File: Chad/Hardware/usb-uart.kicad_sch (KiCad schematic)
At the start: 27 parts, among them J3 USB_C_Receptacle_USB2.0, U3 INTERFACE-CP2102-GMR(QFN28), U6 RT9025-25GSP, U7 LTC4411

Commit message: Implemented design review feedback
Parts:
- C24: value 0.1uF -> 10uF
- renumbered D5 to USBLED1
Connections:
- net +3V3: now also R19.2
- net GND: no longer R19.2
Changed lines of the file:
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@@
+    (stroke (width 0) (type default) (color 0 0 0 0))
+  )
+  (wire (pts (xy 210.82 120.65) (xy 210.82 125.73))
     (stroke (width 0) (type default) (color 0 0 0 0))
   )
@@
   )
   (wire (pts (xy 208.28 102.87) (xy 215.9 102.87))
+    (stroke (width 0) (type default) (color 0 0 0 0))
+  )
+  (wire (pts (xy 210.82 125.73) (xy 205.74 125.73))
     (stroke (width 0) (type default) (color 0 0 0 0))
   )
@@
   (symbol (lib_id "Device:LED_Small") (at 162.56 92.71 180) (unit 1)
     (in_bom yes) (on_board yes)
-    (property "Reference" "D5" (id 0) (at 162.56 87.503 0))
+    (property "Reference" "USBLED1" (id 0) (at 162.56 87.503 0))
     (property "Value" "USB_LED" (id 1) (at 162.56 89.8144 0))
     (property "Footprint" "LED_SMD:LED_0603_1608Metric" (id 2) (at 162.56 92.71 90)
@@
     (pin "1")
   )
-  (symbol (lib_id "power:GND") (at 210.82 120.65 0) (unit 1)
-    (in_bom yes) (on_board yes) (fields_autoplaced)
-    (property "Reference" "#PWR013" (id 0) (at 210.82 127 0)
-      (effects (font (size 1.27 1.27)) hide)
-    )
-    (property "Value" "GND" (id 1) (at 210.82 125.73 0))
-    (property "Footprint" "" (id 2) (at 210.82 120.65 0)
-      (effects (font (size 1.27 1.27)) hide)
-    )
-    (property "Datasheet" "" (id 3) (at 210.82 120.65 0)
-      (effects (font (size 1.27 1.27)) hide)
-    )
-    (pin "1")
-  )
   (symbol (lib_id "Device:R_Small") (at 219.71 115.57 0) (unit 1)
     (in_bom yes) (on_board yes)
@@
     (pin "2")
   )
+  (symbol (lib_id "power:+3.3V") (at 205.74 125.73 0) (unit 1)
+    (in_bom yes) (on_board yes) (fields_autoplaced)
+    (property "Reference" "#PWR0115" (id 0) (at 205.74 129.54 0)
+      (effects (font (size 1.27 1.27)) hide)
+    )
+    (property "Value" "+3.3V" (id 1) (at 205.74 122.1542 0))
+    (property "Footprint" "" (id 2) (at 205.74 125.73 0)
+      (effects (font (size 1.27 1.27)) hide)
+    )
+    (property "Datasheet" "" (id 3) (at 205.74 125.73 0)
+      (effects (font (size 1.27 1.27)) hide)
+    )
+    (pin "1")
+  )
   (symbol (lib_id "Device:C_Small") (at 215.9 106.68 180) (unit 1)
     (in_bom yes) (on_board yes)
@@
       (effects (font (size 1.27 1.27)) (justify right))
     )
-    (property "Value" "0.1uF" (id 1) (at 209.0797 108.2478 0)
-      (effects (font (size 1.27 1.27)) (justify right))
-    )
+    (property "Value" "10uF" (id 1) (at 209.0797 108.2478 0)
+      (effects (font (size 1.27 1.27)) (justify right))
+    )

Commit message: Changed LDO footprint to include exposed pad
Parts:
- U6: footprint Package_SO:SOP-8_3.9x4.9mm_P1.27mm -> iclr:SOIC127P599X175-9N
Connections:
- net GND: now also U6.9 (GND)
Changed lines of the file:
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@@
   (symbol (lib_id "iclr:RT9025-25GSP") (at 198.12 101.6 0) (unit 1)
     (in_bom yes) (on_board yes) (fields_autoplaced)
-    (property "Reference" "U6" (id 0) (at 198.12 95.25 0))
-    (property "Value" "RT9025-25GSP" (id 1) (at 198.12 97.79 0))
-    (property "Footprint" "Package_SO:SOP-8_3.9x4.9mm_P1.27mm" (id 2) (at 198.12 96.52 0)
+    (property "Reference" "U6" (id 0) (at 198.12 96.7572 0))
+    (property "Value" "RT9025-25GSP" (id 1) (at 198.12 99.2941 0))
+    (property "Footprint" "iclr:SOIC127P599X175-9N" (id 2) (at 198.12 96.52 0)
       (effects (font (size 1.27 1.27)) hide)
     )
@@
     (pin "7")
     (pin "8")
+    (pin "9")
   )
   (symbol (lib_id "power:GND") (at 219.71 118.11 0) (unit 1)

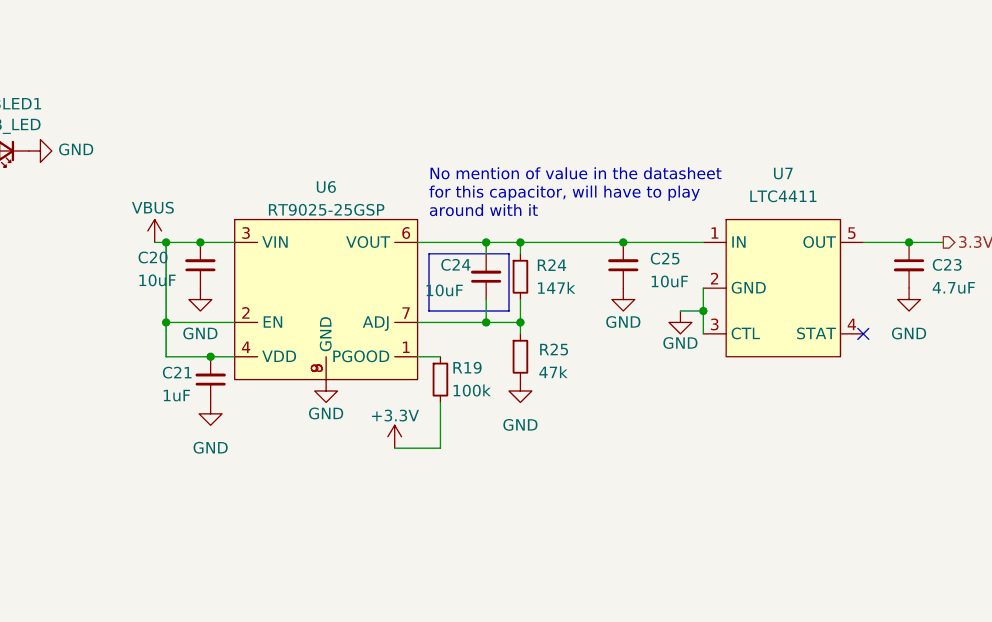
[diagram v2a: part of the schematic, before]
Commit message: change resistor values for new LDO
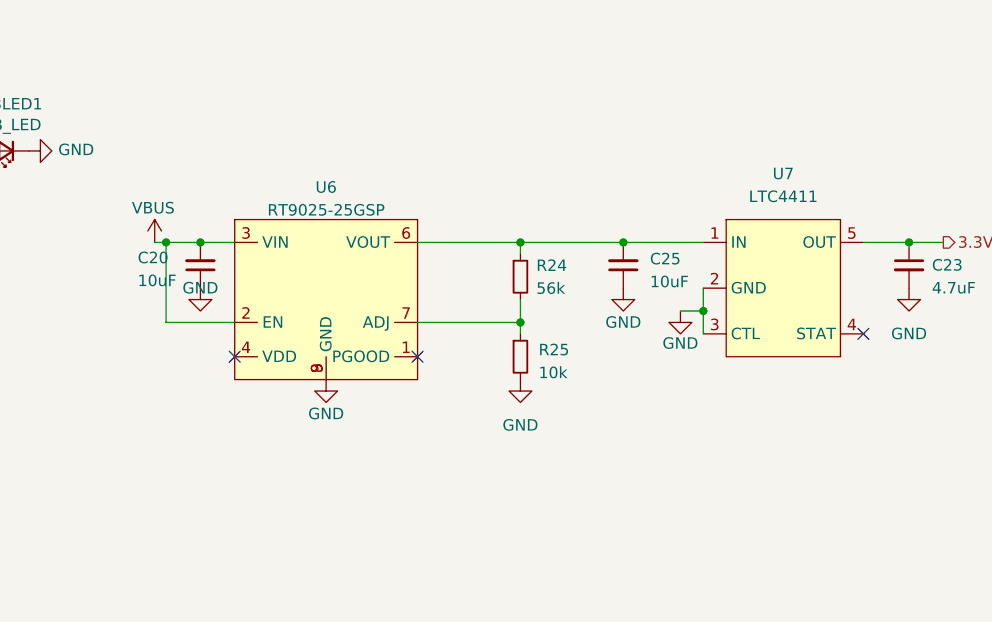
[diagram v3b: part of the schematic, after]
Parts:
- removed C21: 1uF, Capacitor_SMD:C_0603_1608Metric, symbol Device:C_Small
- removed C24: 10uF, Capacitor_SMD:C_0603_1608Metric, symbol Device:C_Small
- removed R19: 100k, Resistor_SMD:R_0603_1608Metric, symbol Device:R_Small
- R24: value 147k -> 56k
- R25: value 47k -> 10k
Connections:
- net VBUS: no longer U6.4 (VDD)
- no-connect marks 21 -> 23
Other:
- note removed: "No mention of value in the datasheet for this capacitor, will have to play around with it"
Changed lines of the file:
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@@
   (junction (at 97.79 52.07) (diameter 0) (color 0 0 0 0)
   )
-  (junction (at 185.2878 115.57) (diameter 0) (color 0 0 0 0)
-  )
   (junction (at 184.15 102.87) (diameter 0) (color 0 0 0 0)
   )
@@
   (junction (at 95.25 52.07) (diameter 0) (color 0 0 0 0)
   )
-  (junction (at 180.34 111.76) (diameter 0) (color 0 0 0 0)
-  )
   (junction (at 102.87 54.61) (diameter 0) (color 0 0 0 0)
   )
   (junction (at 219.71 102.87) (diameter 0) (color 0 0 0 0)
   )
-  (junction (at 215.9 102.87) (diameter 0) (color 0 0 0 0)
-  )
   (junction (at 111.76 44.45) (diameter 0) (color 0 0 0 0)
   )
@@
   )
   (junction (at 113.03 54.61) (diameter 0) (color 0 0 0 0)
-  )
-  (junction (at 215.9 111.76) (diameter 0) (color 0 0 0 0)
   )
   (no_connect (at 161.29 52.07))
@@
   (no_connect (at 161.29 54.61))
   (no_connect (at 115.57 116.84))
+  (no_connect (at 208.28 115.57))
+  (no_connect (at 187.96 115.57))
   (no_connect (at 135.89 26.67))
   (no_connect (at 148.59 67.31))
@@
     (stroke (width 0) (type default) (color 0 0 0 0))
   )
-  (wire (pts (xy 210.82 120.65) (xy 210.82 125.73))
-    (stroke (width 0) (type default) (color 0 0 0 0))
-  )
   (wire (pts (xy 113.03 58.42) (xy 113.03 54.61))
     (stroke (width 0) (type default) (color 0 0 0 0))
@@
     (stroke (width 0) (type default) (color 0 0 0 0))
   )
-  (polyline (pts (xy 209.55 104.14) (xy 218.44 104.14))
-    (stroke (width 0) (type default) (color 0 0 0 0))
-  )
   (wire (pts (xy 107.95 63.5) (xy 107.95 64.77))
     (stroke (width 0) (type default) (color 0 0 0 0))
   )
-  (wire (pts (xy 185.2878 115.57) (xy 187.96 115.57))
-    (stroke (width 0) (type default) (color 0 0 0 0))
-  )
   (wire (pts (xy 96.52 127) (xy 96.52 130.81))
     (stroke (width 0) (type default) (color 0 0 0 0))
@@
     (stroke (width 0) (type default) (color 0 0 0 0))
   )
-  (wire (pts (xy 208.28 111.76) (xy 215.9 111.76))
-    (stroke (width 0) (type default) (color 0 0 0 0))
-  )
   (wire (pts (xy 115.57 102.87) (xy 115.57 101.6))
     (stroke (width 0) (type default) (color 0 0 0 0))
   )
-  (wire (pts (xy 180.34 111.76) (xy 180.34 115.57))
-    (stroke (width 0) (type default) (color 0 0 0 0))
-  )
-  (wire (pts (xy 180.34 115.57) (xy 185.2878 115.57))
-    (stroke (width 0) (type default) (color 0 0 0 0))
-  )
   (wire (pts (xy 115.57 102.87) (xy 116.84 102.87))
     (stroke (width 0) (type default) (color 0 0 0 0))
@@
     (stroke (width 0) (type default) (color 0 0 0 0))
   )
-  (wire (pts (xy 215.9 102.87) (xy 219.71 102.87))
+  (wire (pts (xy 208.28 102.87) (xy 219.71 102.87))
     (stroke (width 0) (type default) (color 0 0 0 0))
   )
@@
     (stroke (width 0) (type default) (color 0 0 0 0))
   )
-  (wire (pts (xy 208.28 115.57) (xy 210.82 115.57))
-    (stroke (width 0) (type default) (color 0 0 0 0))
-  )
-  (wire (pts (xy 215.9 111.76) (xy 219.71 111.76))
+  (wire (pts (xy 208.28 111.76) (xy 219.71 111.76))
     (stroke (width 0) (type default) (color 0 0 0 0))
   )
@@
     (stroke (width 0) (type default) (color 0 0 0 0))
   )
-  (wire (pts (xy 215.9 102.87) (xy 215.9 104.14))
-    (stroke (width 0) (type default) (color 0 0 0 0))
-  )
   (wire (pts (xy 115.57 93.98) (xy 120.65 93.98))
     (stroke (width 0) (type default) (color 0 0 0 0))
@@
     (stroke (width 0) (type default) (color 0 0 0 0))
   )
-  (wire (pts (xy 208.28 102.87) (xy 215.9 102.87))
-    (stroke (width 0) (type default) (color 0 0 0 0))
-  )
-  (wire (pts (xy 210.82 125.73) (xy 205.74 125.73))
-    (stroke (width 0) (type default) (color 0 0 0 0))
-  )
   (wire (pts (xy 133.35 26.67) (xy 133.35 19.05))
     (stroke (width 0) (type default) (color 0 0 0 0))
   )
-  (polyline (pts (xy 218.44 110.49) (xy 218.44 104.14))
-    (stroke (width 0) (type default) (color 0 0 0 0))
-  )
-  (polyline (pts (xy 209.55 110.49) (xy 218.44 110.49))
-    (stroke (width 0) (type default) (color 0 0 0 0))
-  )
   (wire (pts (xy 184.15 102.87) (xy 187.96 102.87))
     (stroke (width 0) (type default) (color 0 0 0 0))
@@
     (stroke (width 0) (type default) (color 0 0 0 0))
   )
-  (polyline (pts (xy 209.55 104.14) (xy 209.55 110.49))
-    (stroke (width 0) (type default) (color 0 0 0 0))
-  )
   (wire (pts (xy 115.57 106.68) (xy 115.57 107.95))
     (stroke (width 0) (type default) (color 0 0 0 0))
@@
     (stroke (width 0) (type default) (color 0 0 0 0))
   )
-  (wire (pts (xy 215.9 109.22) (xy 215.9 111.76))
-    (stroke (width 0) (type default) (color 0 0 0 0))
-  )
   (wire (pts (xy 118.11 99.06) (xy 120.65 99.06))
     (stroke (width 0) (type default) (color 0 0 0 0))
@@
   (wire (pts (xy 44.45 99.06) (xy 52.07 99.06))
     (stroke (width 0) (type default) (color 0 0 0 0))
-  )
-  (text "No mention of value in the datasheet \nfor this capacitor, will have to play\naround with it\n"
-    (at 209.55 100.33 0)
-    (effects (font (size 1.27 1.27)) (justify left bottom))
   )
   (label "Data+" (at 134.62 134.62 90)
@@
     (pin "2")
   )
-  (symbol (lib_id "Device:R_Small") (at 210.82 118.11 0) (unit 1)
-    (in_bom yes) (on_board yes)
-    (property "Reference" "R19" (id 0) (at 212.09 116.84 0)
-      (effects (font (size 1.27 1.27)) (justify left))
-    )
-    (property "Value" "100k" (id 1) (at 212.09 119.38 0)
-      (effects (font (size 1.27 1.27)) (justify left))
-    )
-    (property "Footprint" "Resistor_SMD:R_0603_1608Metric" (id 2) (at 210.82 118.11 0)
-      (effects (font (size 1.27 1.27)) hide)
-    )
-    (property "Datasheet" "~" (id 3) (at 210.82 118.11 0)
-      (effects (font (size 1.27 1.27)) hide)
-    )
-    (pin "1")
-    (pin "2")
-  )
   (symbol (lib_id "Device:R_Small") (at 128.27 69.85 90) (unit 1)
     (in_bom yes) (on_board yes)
@@
     (pin "2")
   )
-  (symbol (lib_id "power:GND") (at 185.2878 120.65 0) (unit 1)
-    (in_bom yes) (on_board yes) (fields_autoplaced)
-    (property "Reference" "#PWR08" (id 0) (at 185.2878 127 0)
-      (effects (font (size 1.27 1.27)) hide)
-    )
-    (property "Value" "GND" (id 1) (at 185.2878 125.73 0))
-    (property "Footprint" "" (id 2) (at 185.2878 120.65 0)
-      (effects (font (size 1.27 1.27)) hide)
-    )
-    (property "Datasheet" "" (id 3) (at 185.2878 120.65 0)
-      (effects (font (size 1.27 1.27)) hide)
-    )
-    (pin "1")
-  )
   (symbol (lib_id "power:VBUS") (at 123.19 69.85 0) (unit 1)
     (in_bom yes) (on_board yes)
@@
     (pin "1")
   )
-  (symbol (lib_id "Device:C_Small") (at 185.2878 118.11 180) (unit 1)
-    (in_bom yes) (on_board yes)
-    (property "Reference" "C21" (id 0) (at 179.8846 117.3862 0)
-      (effects (font (size 1.27 1.27)) (justify right))
-    )
-    (property "Value" "1uF" (id 1) (at 179.8846 119.9262 0)
-      (effects (font (size 1.27 1.27)) (justify right))
-    )
-    (property "Footprint" "Capacitor_SMD:C_0603_1608Metric" (id 2) (at 185.2878 118.11 0)
-      (effects (font (size 1.27 1.27)) hide)
-    )
-    (property "Datasheet" "~" (id 3) (at 185.2878 118.11 0)
-      (effects (font (size 1.27 1.27)) hide)
-    )
-    (pin "1")
-    (pin "2")
-  )
   (symbol (lib_id "power:GND") (at 237.49 110.49 0) (unit 1)
     (in_bom yes) (on_board yes)
@@
       (effects (font (size 1.27 1.27)) (justify left))
     )
-    (property "Value" "47k" (id 1) (at 221.724 117.3597 0)
+    (property "Value" "10k" (id 1) (at 221.724 117.3597 0)
       (effects (font (size 1.27 1.27)) (justify left))
     )
@@
       (effects (font (size 1.27 1.27)) (justify left))
     )
-    (property "Value" "147k" (id 1) (at 221.4667 107.9905 0)
+    (property "Value" "56k" (id 1) (at 221.4667 107.9905 0)
       (effects (font (size 1.27 1.27)) (justify left))
     )
@@
     (pin "2")
   )
-  (symbol (lib_id "power:+3.3V") (at 205.74 125.73 0) (unit 1)
-    (in_bom yes) (on_board yes) (fields_autoplaced)
-    (property "Reference" "#PWR0115" (id 0) (at 205.74 129.54 0)
-      (effects (font (size 1.27 1.27)) hide)
-    )
-    (property "Value" "+3.3V" (id 1) (at 205.74 122.1542 0))
-    (property "Footprint" "" (id 2) (at 205.74 125.73 0)
-      (effects (font (size 1.27 1.27)) hide)
-    )
-    (property "Datasheet" "" (id 3) (at 205.74 125.73 0)
-      (effects (font (size 1.27 1.27)) hide)
-    )
-    (pin "1")
-  )
-  (symbol (lib_id "Device:C_Small") (at 215.9 106.68 180) (unit 1)
-    (in_bom yes) (on_board yes)
-    (property "Reference" "C24" (id 0) (at 210.82 105.41 0)
-      (effects (font (size 1.27 1.27)) (justify right))
-    )
-    (property "Value" "10uF" (id 1) (at 209.0797 108.2478 0)
-      (effects (font (size 1.27 1.27)) (justify right))
-    )
-    (property "Footprint" "Capacitor_SMD:C_0603_1608Metric" (id 2) (at 215.9 106.68 0)
-      (effects (font (size 1.27 1.27)) hide)
-    )
-    (property "Datasheet" "~" (id 3) (at 215.9 106.68 0)
-      (effects (font (size 1.27 1.27)) hide)
-    )
-    (pin "1")
-    (pin "2")
-  )
   (symbol (lib_id "power:GND") (at 262.89 107.95 0) (unit 1)
     (in_bom yes) (on_board yes) (fields_autoplaced)
@@
   )
   (symbol (lib_id "power:GND") (at 184.15 107.95 0) (unit 1)
-    (in_bom yes) (on_board yes) (fields_autoplaced)
+    (in_bom yes) (on_board yes)
     (property "Reference" "#PWR05" (id 0) (at 184.15 114.3 0)
       (effects (font (size 1.27 1.27)) hide)
     )
-    (property "Value" "GND" (id 1) (at 184.15 113.03 0))
+    (property "Value" "GND" (id 1) (at 184.15 107.95 0))
     (property "Footprint" "" (id 2) (at 184.15 107.95 0)
       (effects (font (size 1.27 1.27)) hide)

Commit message: Chad V2
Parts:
- U6: value RT9025-25GSP -> SC2416H
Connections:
- net GND: now also U3.29 (GND@1)
- no-connect marks 23 -> 22
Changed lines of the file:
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@@
   (no_connect (at 146.05 26.67))
   (no_connect (at 161.29 41.91))
-  (no_connect (at 130.81 26.67))
   (no_connect (at 161.29 44.45))
   (no_connect (at 115.57 119.38))
@@
     (in_bom yes) (on_board yes) (fields_autoplaced)
     (property "Reference" "U6" (id 0) (at 198.12 96.7572 0))
-    (property "Value" "RT9025-25GSP" (id 1) (at 198.12 99.2941 0))
+    (property "Value" "SC2416H" (id 1) (at 198.12 99.2941 0))
     (property "Footprint" "iclr:SOIC127P599X175-9N" (id 2) (at 198.12 96.52 0)
       (effects (font (size 1.27 1.27)) hide)
@@
       (effects (font (size 1.27 1.27)) hide)
     )
+    (pin "1")
+  )
+  (symbol (lib_id "power:GND") (at 130.81 26.67 180) (unit 1)
+    (in_bom yes) (on_board yes) (fields_autoplaced)
+    (property "Reference" "#PWR0115" (id 0) (at 130.81 20.32 0)
+      (effects (font (size 1.27 1.27)) hide)
+    )
+    (property "Value" "GND" (id 1) (at 130.81 23.0942 0))
+    (property "Footprint" "" (id 2) (at 130.81 26.67 0)
+      (effects (font (size 1.27 1.27)) hide)
+    )
+    (property "Datasheet" "" (id 3) (at 130.81 26.67 0)
+      (effects (font (size 1.27 1.27)) hide)
+    )
